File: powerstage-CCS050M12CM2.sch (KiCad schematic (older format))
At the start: 9 parts, among them J12 CONN_02X13, U6 74LVC8T245, U7 74LVC2G04

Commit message: schematic updates for V2; PCB draft layout
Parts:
- removed J12: CONN_02X13, Connect:IDC_Header_Straight_26pins, symbol CONN_02X13
- removed R37: 745C101103 (10k), Resistors_SMD:R_Array_Convex_5x1206, symbol R_ARRAY_8_10
- removed R39: 5k1, Resistors_SMD:R_0603, symbol R_Small
- added Q?: CCS050M12CM2, symbol CCS050M12CM2
- added R? (x6): 10k, Resistors_SMD:R_0603, symbol R_Small
- C25, C26, C27: value 1uF -> 0.1uF
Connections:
- net labels added: BUS+, BUS-, GDRV_RDY_TTL, PHASE_A, PHASE_B, PHASE_C, ~GDRV_RDY
- net labels removed: +15V, FLT_OTP_TTL, PWR_RDY, PWR_RDY_TTL, ~FLT_OTP
- wire segments 52 -> 106
- no-connect marks 3 -> 1
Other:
- note removed: "IDC connector to CGD15FB45P1"
- note removed: "Safety pulldowns"
- moved on the sheet: C25, C26, C27, R38, U6, U7A, U7B

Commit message: progress on V2 schematic
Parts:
- added C? (x16): 1uF, Capacitors_SMD:C_0603, symbol C_Small
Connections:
- net Halfbridge Driver/GATE_H is gone; now on net Halfbridge Driver/GATE_H: Q?.9 (G_CH)
- net Halfbridge Driver/GATE_L is gone; now on net Halfbridge Driver/GATE_L: Q?.7 (G_BL)
- net Halfbridge Driver/SRC_H is gone; now on net Halfbridge Driver/SRC_H: Q?.6 (S_BH)
- net Halfbridge Driver/SRC_L is gone; now on net Halfbridge Driver/SRC_L: Q?.8 (S_BL)
- net BUS+: now also C?.1, C?.1, C?.1, C?.1, C?.1, C?.1, C?.1, C?.1, C?.1, C?.1, C?.1, C?.1, C?.1, C?.1, C?.1, C?.1
- net BUS-: now also C?.2, C?.2, C?.2, C?.2, C?.2, C?.2, C?.2, C?.2, C?.2, C?.2, C?.2, C?.2, C?.2, C?.2, C?.2, C?.2
- net Halfbridge Driver/GATE_H: no longer Q?.1 (G_AH)
- net Halfbridge Driver/GATE_L: no longer Q?.11 (G_CL)
- net Halfbridge Driver/SRC_H: no longer Q?.10 (S_CH)
- net Halfbridge Driver/SRC_L: no longer Q?.12 (S_CL)
- net CCS_NTC_2: now reaches Q?.17
- net CCS_NTC_1: now reaches Q?.18
- new net Halfbridge Driver/GATE_H: Q?.1 (G_AH)
- new net Halfbridge Driver/GATE_L: Q?.11 (G_CL)
- new net Halfbridge Driver/SRC_H: Q?.10 (S_CH)
- new net Halfbridge Driver/SRC_L: Q?.12 (S_CL)

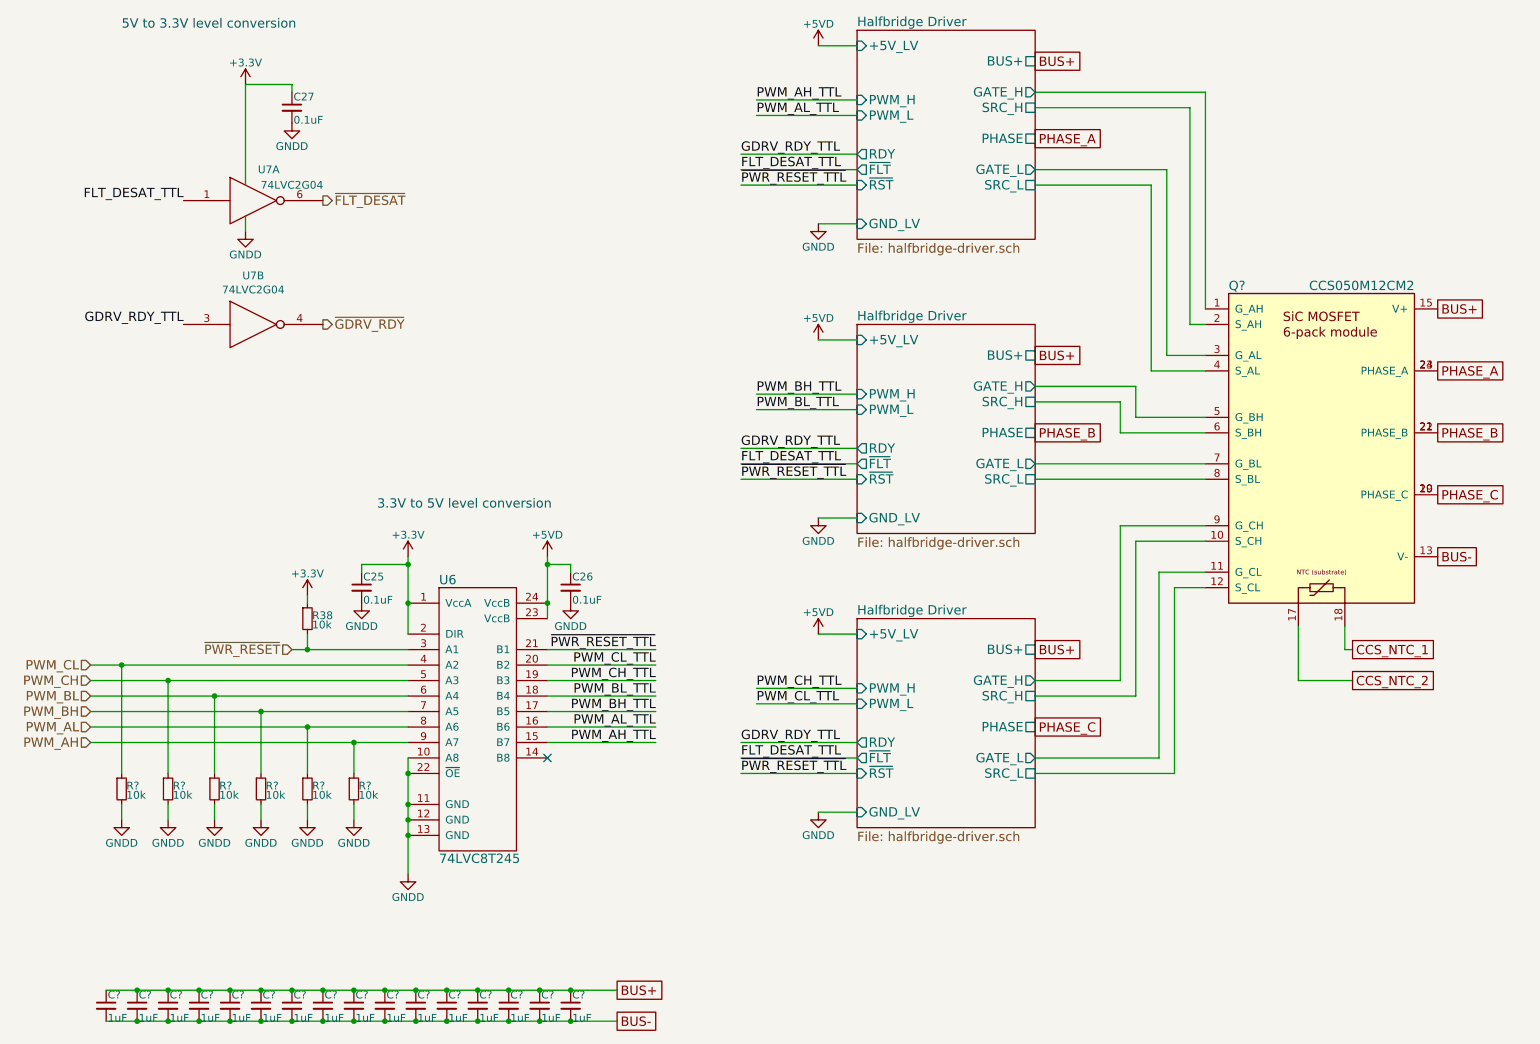
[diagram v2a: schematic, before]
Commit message: V2 schem complete, footprints not assigned
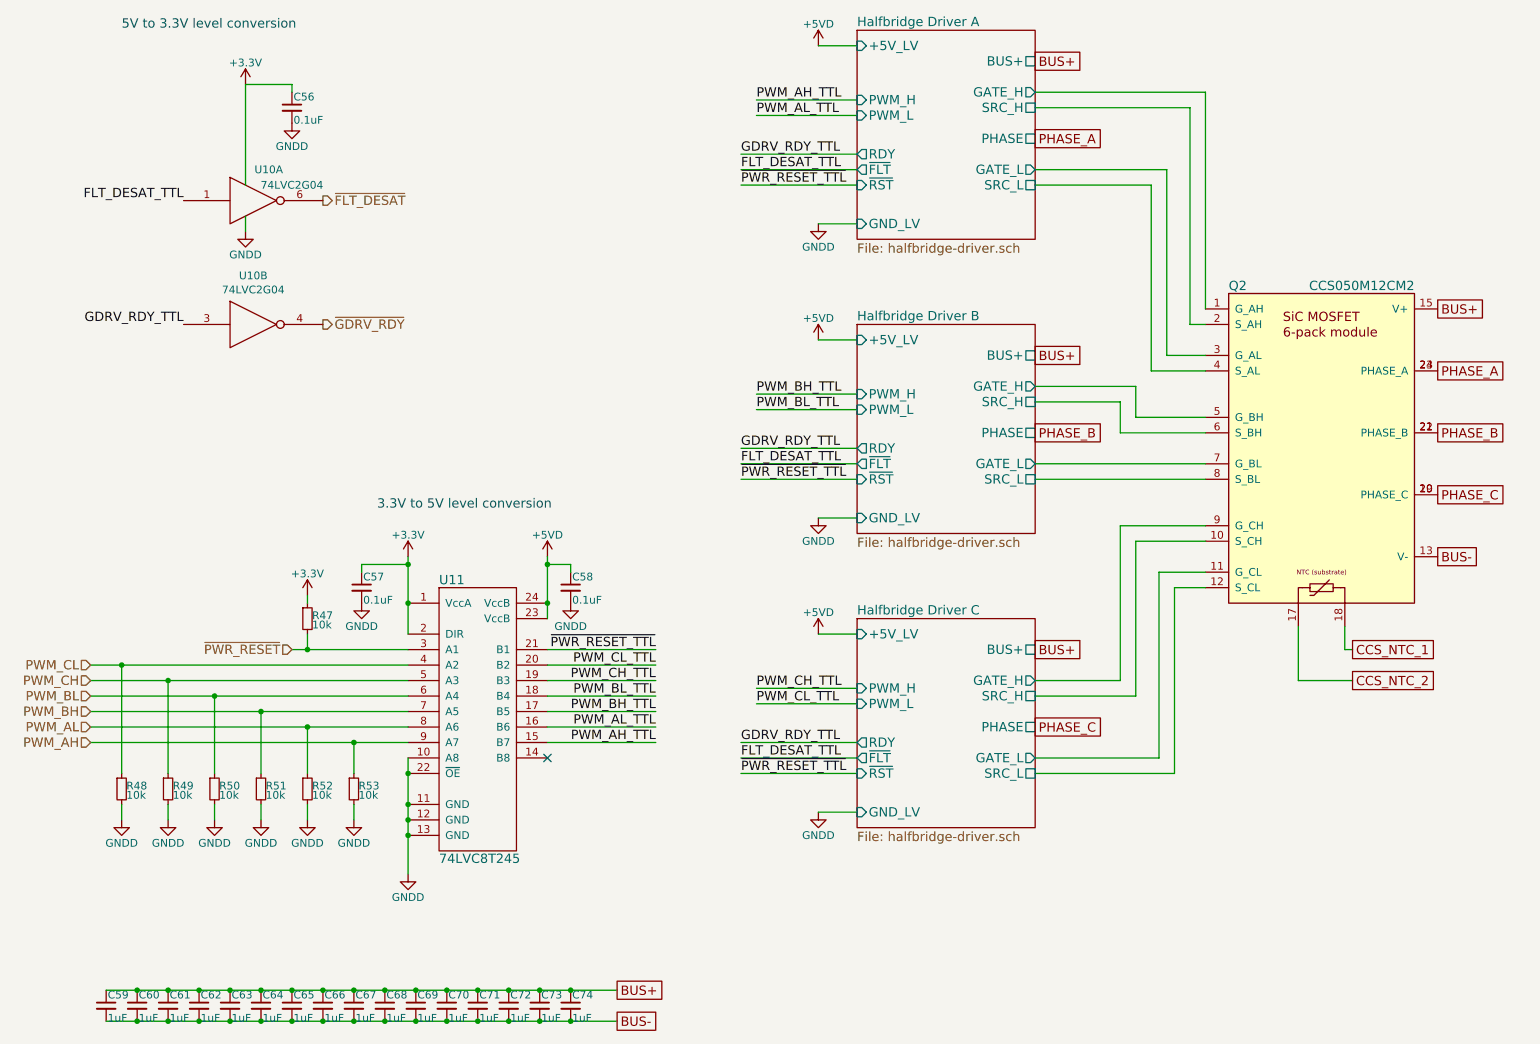
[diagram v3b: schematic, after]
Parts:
- gave numbers to parts that had none: 23
- renumbered C27 to C56, C25 to C57, C26 to C58, R38 to R47, U7 to U10, U6 to U11
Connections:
- net Halfbridge Driver/GATE_H renamed Halfbridge Driver A/GATE_H
- net Halfbridge Driver/GATE_H renamed Halfbridge Driver B/GATE_H
- net Halfbridge Driver/GATE_H renamed Halfbridge Driver C/GATE_H
- net Halfbridge Driver/GATE_L renamed Halfbridge Driver C/GATE_L
- net Halfbridge Driver/GATE_L renamed Halfbridge Driver A/GATE_L
- net Halfbridge Driver/GATE_L renamed Halfbridge Driver B/GATE_L
- net Halfbridge Driver/SRC_H renamed Halfbridge Driver C/SRC_H
- net Halfbridge Driver/SRC_H renamed Halfbridge Driver A/SRC_H
- net Halfbridge Driver/SRC_H renamed Halfbridge Driver B/SRC_H
- net Halfbridge Driver/SRC_L renamed Halfbridge Driver C/SRC_L
- net Halfbridge Driver/SRC_L renamed Halfbridge Driver A/SRC_L
- net Halfbridge Driver/SRC_L renamed Halfbridge Driver B/SRC_L

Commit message: Add TVS protection to signal I/O.  Reannotate. Assign some footprints.
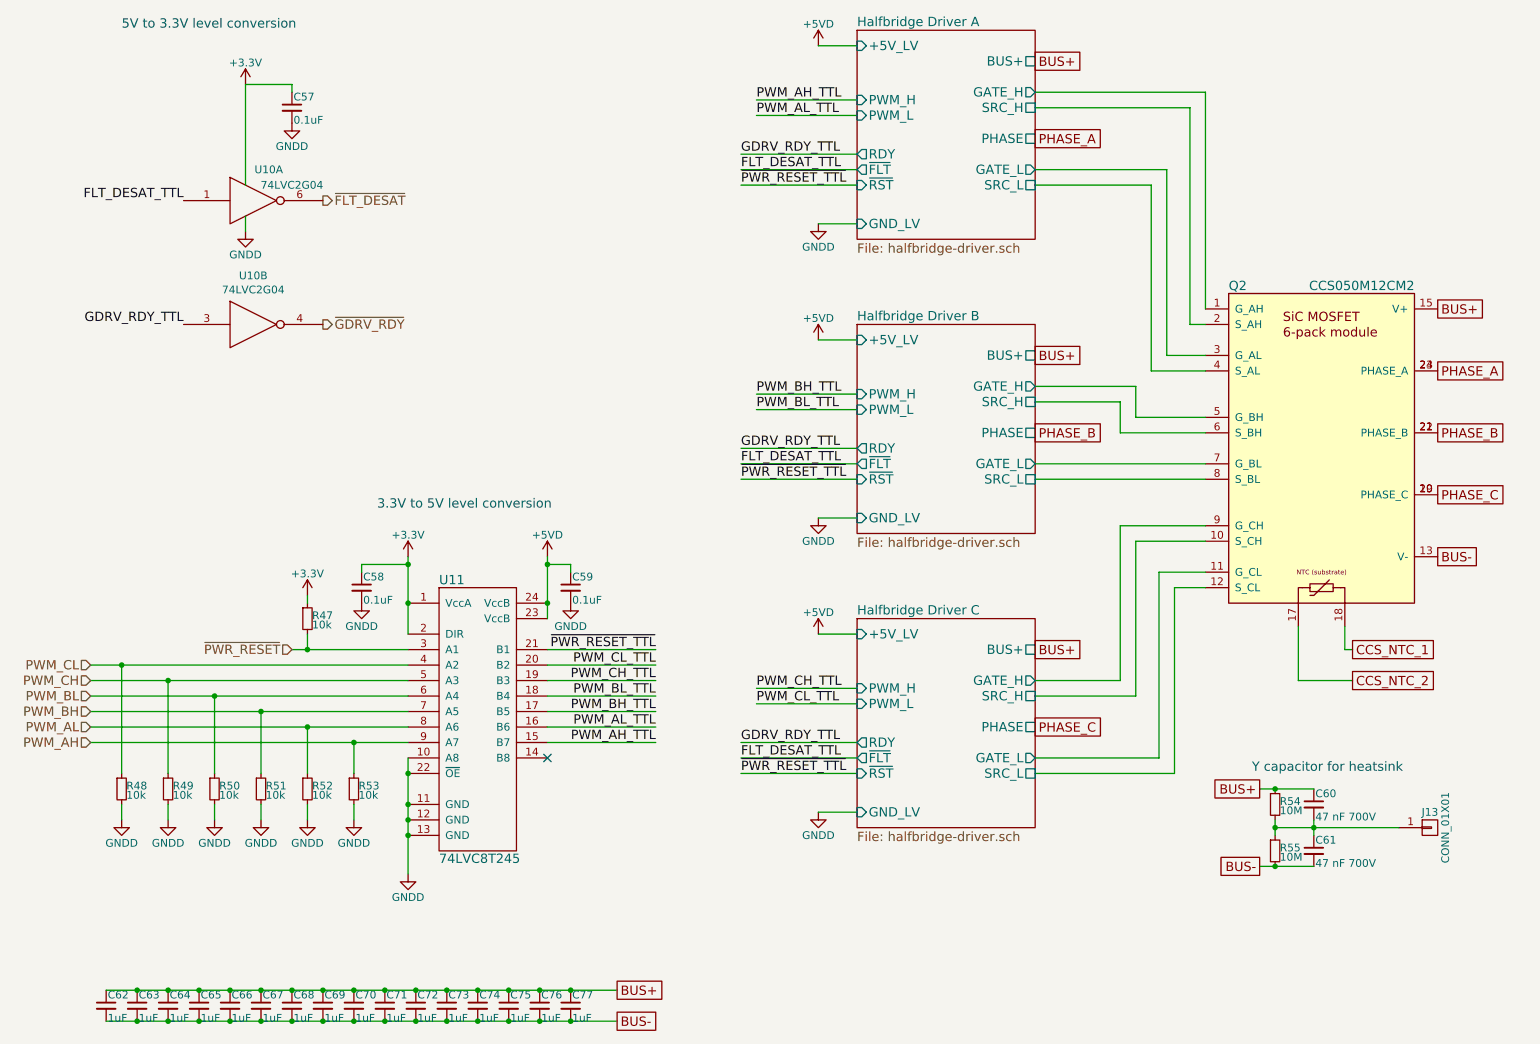
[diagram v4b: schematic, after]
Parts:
- added C60, C61: 47 nF 700V, Capacitors_SMD:C_1210, symbol C_Small
- added J13: CONN_01X01, symbol CONN_01X01
- added R54, R55: 10M, Resistors_SMD:R_0805, symbol R_Small
- renumbered C56 to C57, C57 to C58, C58 to C59, C59 to C62, C60 to C63, C61 to C64, C62 to C65, C63 to C66, C64 to C67, C65 to C68, C66 to C69, C67 to C70, C68 to C71, C69 to C72, C70 to C73, C71 to C74, C72 to C75, C73 to C76, C74 to C77
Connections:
- net BUS+: now also C60.1, R54.1
- net BUS-: now also C61.2, R55.2
- new net: C60.2, C61.1, J13.1 (P1), R54.2, R55.1
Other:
- note added: "Y capacitor for heatsink"
